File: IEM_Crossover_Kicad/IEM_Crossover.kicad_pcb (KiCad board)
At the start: 2 copper layers, 5 parts, among them J1 0.78mm 2-pin

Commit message: finished layout
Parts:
- added B1: C_Small, Capacitor_SMD:C_0805_2012Metric, F.Cu at (137.8, 96.4)
- added B2: C_Small, Capacitor_SMD:C_0805_2012Metric, F.Cu at (138.1, 98.4)
- added C1: C_Small, Capacitor_SMD:C_0805_2012Metric, F.Cu at (137.8, 100.4)
- added C2: C_Small, Capacitor_SMD:C_0805_2012Metric, F.Cu at (138.8, 102.4)
- added D1: C_Small, Capacitor_SMD:C_0805_2012Metric, F.Cu at (139.2, 104.4)
- added D2: C_Small, Capacitor_SMD:C_0805_2012Metric, F.Cu at (140.1, 106.3)
- added DR2: Speaker, Library:IEM_Driver_1x2_Pad, F.Cu at (146.7, 97.5)
- added DR3: Speaker, Library:IEM_Driver_1x2_Pad, F.Cu at (145.8, 100.6)
- added DR4: Speaker, Library:IEM_Driver_1x2_Pad, F.Cu at (144.0, 103.1)
- added R2: R_Small, Capacitor_SMD:C_0805_2012Metric, F.Cu at (142.6, 96.8)
- added R3: R_Small, Capacitor_SMD:C_0805_2012Metric, F.Cu at (141.8, 100.4)
- added R4: R_Small, Capacitor_SMD:C_0805_2012Metric, F.Cu at (141.8, 103.3)
- moved J1 21.0 mm to (134.4, 98.5), turned to -70 degrees
- moved A1 16.2 mm to (138.1, 92.5)
- moved DR1 14.7 mm to (145.5, 94.5), turned to 155 degrees
- moved R1 14.3 mm to (141.7, 94.0), turned to -15 degrees
- moved A2 13.1 mm to (138.1, 94.5), turned to 0 degrees
- renumbered Z1 to A1, Z2 to A2, D1 to DR1
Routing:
- net Net-(J1-Pin_1): track 0.00 -> 17.9 mm
- net GND: track 0.00 -> 10.5 mm, vias 0 -> 13
- net Net-(B1-Pad2): track 0.00 -> 5.13 mm
- net Net-(C1-Pad2): track 0.00 -> 4.50 mm
- net Net-(D1-Pad2): track 0.00 -> 3.82 mm
- net Net-(A1-Pad2): track 0.00 -> 3.66 mm
- net Net-(DR2-Pad1): track 0.00 -> 3.50 mm
- net Net-(DR1-Pad1): track 0.00 -> 3.40 mm
- net Net-(DR3-Pad1): track 0.00 -> 3.18 mm
- net Net-(DR4-Pad1): track 0.00 -> 2.47 mm
- added copper zone on B.Cu, net GND
- added copper zone on F.Cu, net GND
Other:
- board outline added: 16 x 18.1 mm
- board text added: "1"
- board text added: "2"
- board text added: "3"

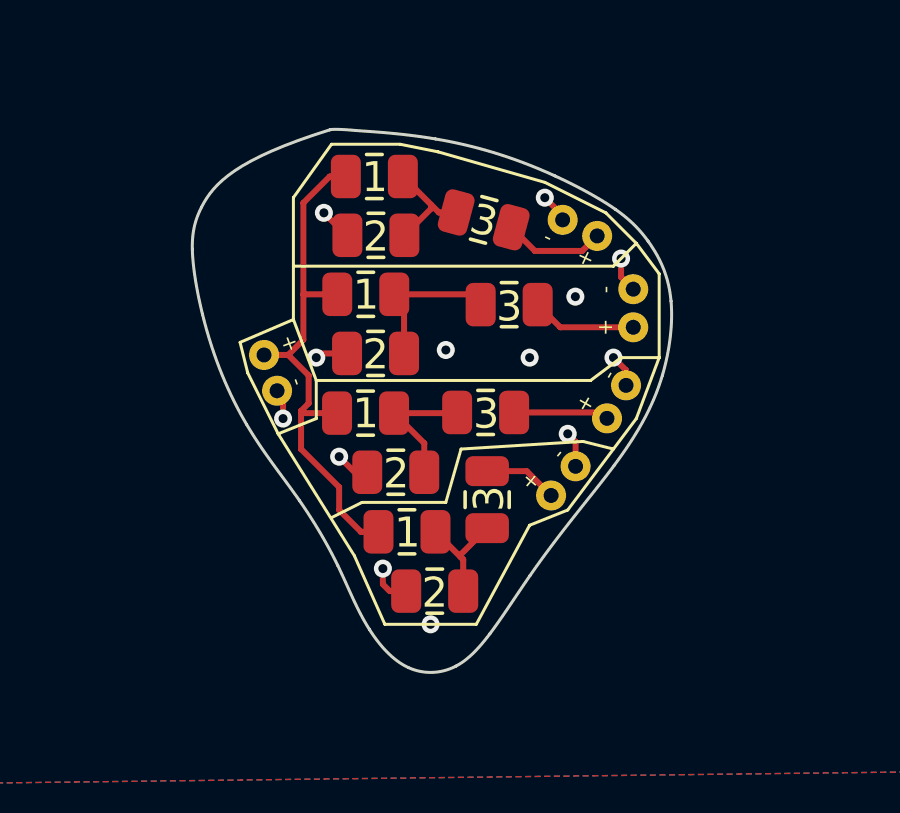
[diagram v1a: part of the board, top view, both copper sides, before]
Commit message: widened BA driver footprints, optimized ground pour and vias
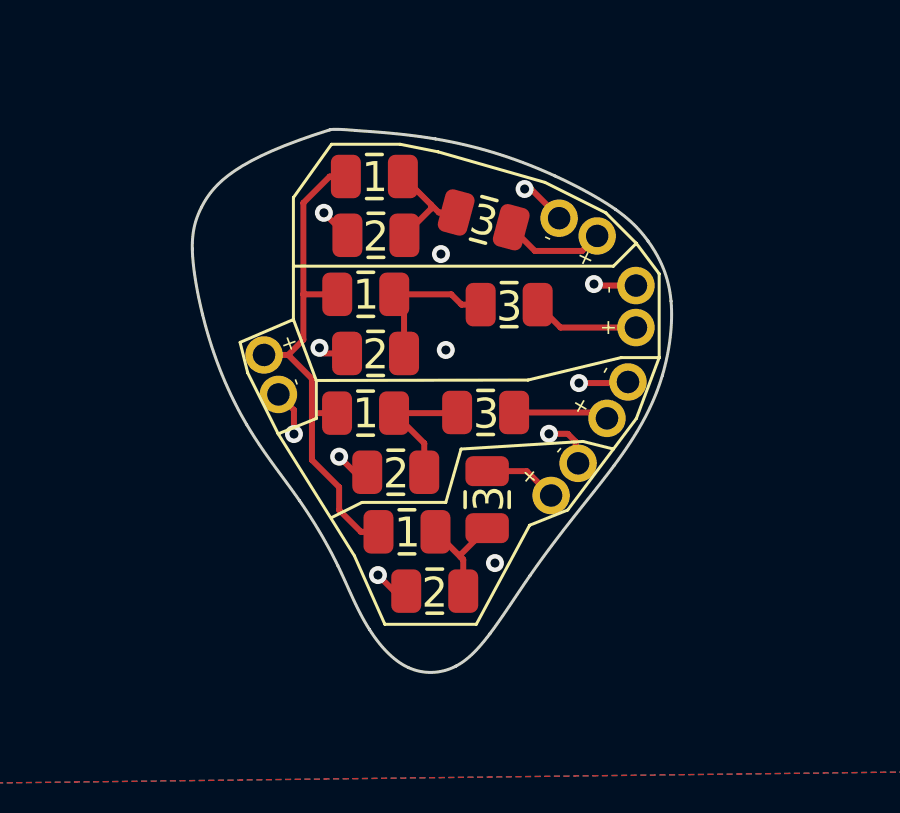
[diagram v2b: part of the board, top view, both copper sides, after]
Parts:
- moved DR2 0.09 mm to (146.8, 97.5)
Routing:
- net GND: track 10.5 -> 12.5 mm, vias 13 -> 12
- net Net-(J1-Pin_1): track 17.9 -> 17.3 mm
